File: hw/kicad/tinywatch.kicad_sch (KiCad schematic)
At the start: 18 parts, among them J1 Conn_01x04, J2 Conn_01x30, SW1 SW_Push, SW2 SW_Push, SW3 SW_Push, U1 ATtiny1614-SS

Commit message: R2 hardware
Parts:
- removed R1: 4k7, Resistor_SMD:R_0603_1608Metric_Pad0.98x0.95mm_HandSolder, symbol Device:R
- added C10, C9: 8.2p, Capacitor_SMD:C_0603_1608Metric_Pad1.08x0.95mm_HandSolder, symbol Device:C
- added J3, J4: Conn_01x01_Pin, Connector_Wire:SolderWire-0.25sqmm_1x01_D0.65mm_OD1.7mm, symbol Connector:Conn_01x01_Pin
- added Y1: 32.768 kHz, Crystal:Crystal_DS10_D1.0mm_L4.3mm_Horizontal, symbol Device:Crystal
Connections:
- net GND: now also C10.1, C9.2, J4.1 (Pin_1)
- net VCC: now also J3.1 (Pin_1)
- net VCCQ: now also U1.2 (PA4); no longer U1.11 (PA1)
- net at J1.1 (Pin_1): now also U1.12 (PA2); no longer U1.6 (PB3)
- net at J1.2 (Pin_2): now also U1.11 (PA1); no longer U1.7 (PB2)
- net at J1.3 (Pin_3): now also U1.10 (~{RESET}/PA0)
- new net: C9.1, U1.6 (PB3), Y1.1
- new net: C10.2, U1.7 (PB2), Y1.2
- no-connect marks 1 -> 2
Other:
- moved on the sheet: J1

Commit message: Updated BOM and README
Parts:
- D1: footprint Diode_SMD:D_SOD-110 -> Diode_SMD:D_SOD-123
- J3, J4: now left out of the parts list
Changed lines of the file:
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@@
 	(paper "A4")
 	(junction
+		(at 191.77 71.12)
+		(diameter 0)
+		(color 0 0 0 0)
+	)
+	(junction
 		(at 60.96 78.74)
 		(diameter 0)
@@
 	)
 	(junction
-		(at 191.77 63.5)
-		(diameter 0)
-		(color 0 0 0 0)
-	)
-	(junction
-		(at 191.77 71.12)
+		(at 191.77 101.6)
 		(diameter 0)
 		(color 0 0 0 0)
 	)
 	(junction
-		(at 191.77 101.6)
+		(at 191.77 63.5)
 		(diameter 0)
 		(color 0 0 0 0)
@@
 	(wire
 		(pts
-			(xy 181.61 71.12) (xy 191.77 71.12)
-		)
-		(stroke
-			(width 0)
-			(type default)
-		)
-	)
-	(wire
-		(pts
 			(xy 199.39 106.68) (xy 220.98 106.68)
 		)
@@
 	(wire
 		(pts
+			(xy 191.77 71.12) (xy 205.74 71.12)
+		)
+		(stroke
+			(width 0)
+			(type default)
+		)
+	)
+	(wire
+		(pts
 			(xy 86.36 71.12) (xy 80.01 71.12)
 		)
@@
 	(wire
 		(pts
-			(xy 191.77 71.12) (xy 205.74 71.12)
+			(xy 181.61 71.12) (xy 191.77 71.12)
 		)
 		(stroke
@@
 		(unit 1)
 		(exclude_from_sim no)
-		(in_bom yes)
+		(in_bom no)
 		(on_board yes)
 		(dnp no)
@@
 	)
 	(symbol
+		(lib_name "1N4148W_1")
+		(lib_id "Diode:1N4148W")
+		(at 191.77 67.31 270)
+		(unit 1)
+		(exclude_from_sim no)
+		(in_bom yes)
+		(on_board yes)
+		(dnp no)
+		(fields_autoplaced yes)
+		(property "Reference" "D1"
+			(at 194.31 66.0399 90)
+			(effects
+				(font
+					(size 1.27 1.27)
+				)
+				(justify left)
+			)
+		)
+		(property "Value" "1N4148W"
+			(at 194.31 68.5799 90)
+			(effects
+				(font
+					(size 1.27 1.27)
+				)
+				(justify left)
+			)
+		)
+		(property "Footprint" "Diode_SMD:D_SOD-123"
+			(at 187.325 67.31 0)
+			(effects
+				(font
+					(size 1.27 1.27)
+				)
+				(hide yes)
+			)
+		)
+		(property "Datasheet" "https://www.vishay.com/docs/85748/1n4148w.pdf"
+			(at 191.77 67.31 0)
+			(effects
+				(font
+					(size 1.27 1.27)
+				)
+				(hide yes)
+			)
+		)
+		(property "Description" "75V 0.15A Fast Switching Diode, SOD-123"
+			(at 191.77 67.31 0)
+			(effects
+				(font
+					(size 1.27 1.27)
+				)
+				(hide yes)
+			)
+		)
+		(property "Sim.Device" "D"
+			(at 191.77 67.31 0)
+			(effects
+				(font
+					(size 1.27 1.27)
+				)
+				(hide yes)
+			)
+		)
+		(property "Sim.Pins" "1=K 2=A"
+			(at 191.77 67.31 0)
+			(effects
+				(font
+					(size 1.27 1.27)
+				)
+				(hide yes)
+			)
+		)
+		(pin "2"
+		)
+		(pin "1"
+		)
+		(instances
+			(project "tinywatch"
+				(path "/645abe9d-7b27-45bb-9d9d-6ce483163c39"
+					(reference "D1")
+					(unit 1)
+				)
+			)
+		)
+	)
+	(symbol
 		(lib_id "power:GND")
 		(at 220.98 99.06 270)
@@
 	)
 	(symbol
-		(lib_id "Diode:1N4148W")
-		(at 191.77 67.31 270)
-		(unit 1)
-		(exclude_from_sim no)
-		(in_bom yes)
-		(on_board yes)
-		(dnp no)
-		(fields_autoplaced yes)
-		(property "Reference" "D1"
-			(at 194.31 66.0399 90)
-			(effects
-				(font
-					(size 1.27 1.27)
-				)
-				(justify left)
-			)
-		)
-		(property "Value" "1N4148W"
-			(at 194.31 68.5799 90)
-			(effects
-				(font
-					(size 1.27 1.27)
-				)
-				(justify left)
-			)
-		)
-		(property "Footprint" "Diode_SMD:D_SOD-110"
-			(at 187.325 67.31 0)
-			(effects
-				(font
-					(size 1.27 1.27)
-				)
-				(hide yes)
-			)
-		)
-		(property "Datasheet" "https://www.vishay.com/docs/85748/1n4148w.pdf"
-			(at 191.77 67.31 0)
-			(effects
-				(font
-					(size 1.27 1.27)
-				)
-				(hide yes)
-			)
-		)
-		(property "Description" ""
-			(at 191.77 67.31 0)
-			(effects
-				(font
-					(size 1.27 1.27)
-				)
-				(hide yes)
-			)
-		)
-		(pin "1"
-		)
-		(pin "2"
-		)
-		(instances
-			(project ""
-				(path "/645abe9d-7b27-45bb-9d9d-6ce483163c39"
-					(reference "D1")
-					(unit 1)
-				)
-			)
-		)
-	)
-	(symbol
 		(lib_name "GND_1")
 		(lib_id "power:GND")
@@
 		(unit 1)
 		(exclude_from_sim no)
-		(in_bom yes)
+		(in_bom no)
 		(on_board yes)
 		(dnp no)

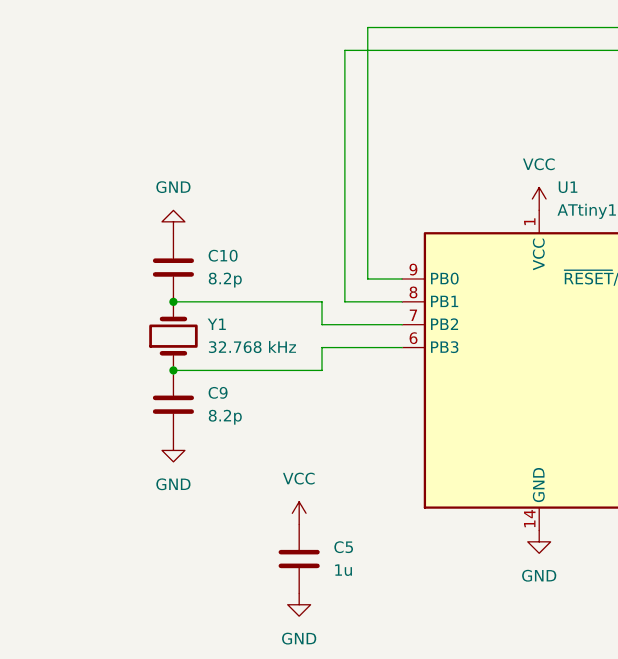
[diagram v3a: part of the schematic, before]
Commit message: Replaced the crystal with a more precise TXCO
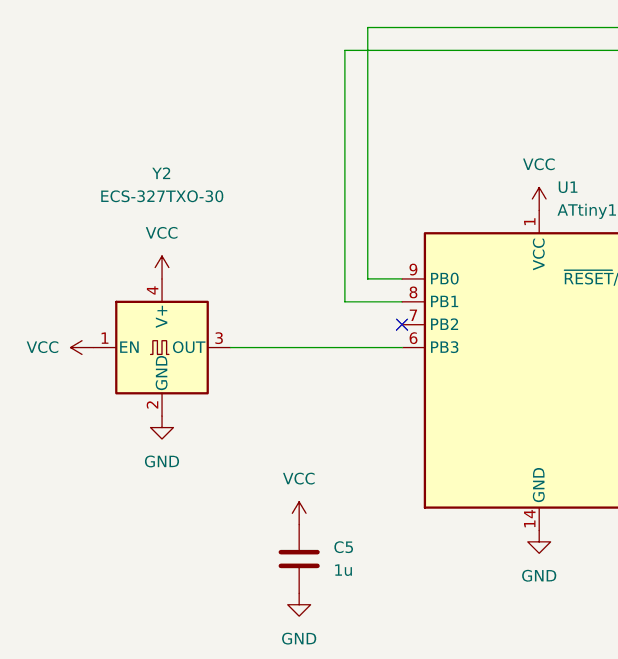
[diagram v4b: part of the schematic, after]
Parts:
- removed C10, C9: 8.2p, Capacitor_SMD:C_0603_1608Metric_Pad1.08x0.95mm_HandSolder, symbol Device:C
- removed Y1: 32.768 kHz, Crystal:Crystal_DS10_D1.0mm_L4.3mm_Horizontal, symbol Device:Crystal
- added Y2: ECS-327TXO-30, Oscillator:Oscillator_SMD_EuroQuartz_XO32-4Pin_3.2x2.5mm, symbol Oscillator:XO32
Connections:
- net GND: now also Y2.2 (GND)
- net VCC: now also Y2.1 (EN), Y2.4 (V+)
- net at U1.6 (PB3): now also Y2.3 (OUT)
- no-connect marks 2 -> 3

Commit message: Replaced TXCO footprint with a more solderable variant
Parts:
- Y2: footprint Oscillator:Oscillator_SMD_EuroQuartz_XO32-4Pin_3.2x2.5mm -> Oscillator:Oscillator_SMD_Abracon_ASE-4Pin_3.2x2.5mm
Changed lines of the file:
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@@
 			)
 		)
-		(property "Footprint" "Oscillator:Oscillator_SMD_EuroQuartz_XO32-4Pin_3.2x2.5mm"
+		(property "Footprint" "Oscillator:Oscillator_SMD_Abracon_ASE-4Pin_3.2x2.5mm"
 			(at 77.47 85.09 0)
 			(effects

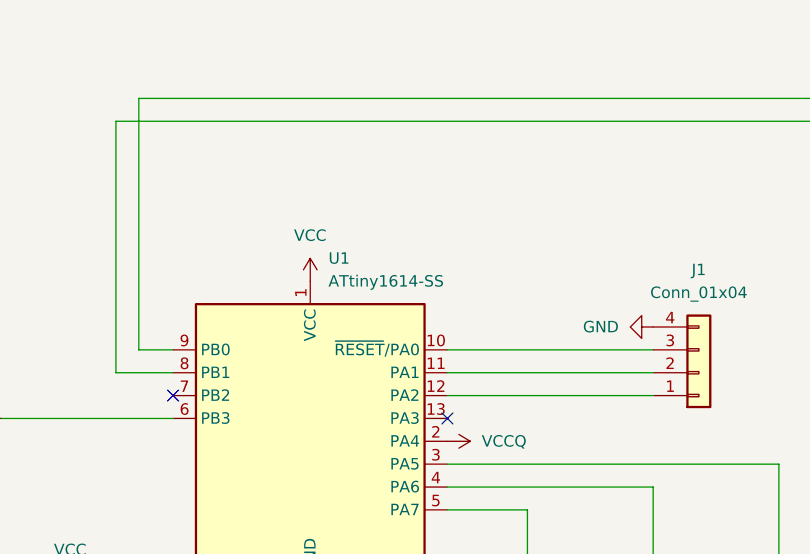
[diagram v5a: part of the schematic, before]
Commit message: Updated to ATtiny3224
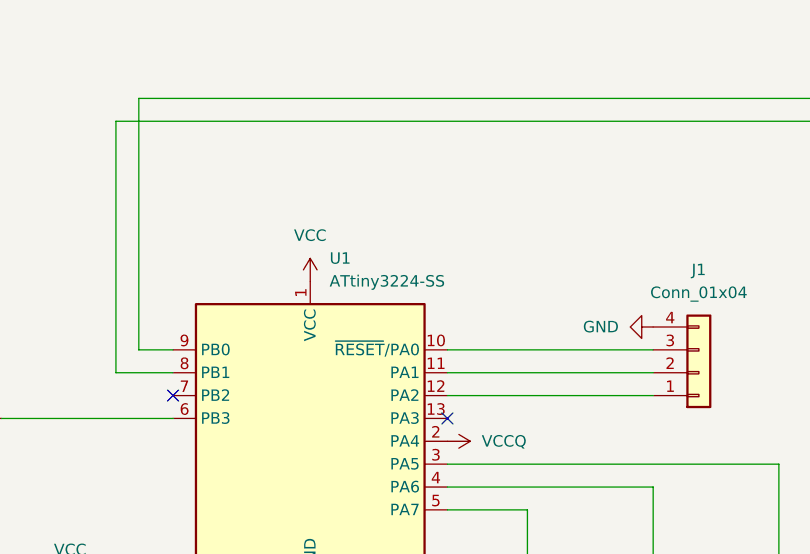
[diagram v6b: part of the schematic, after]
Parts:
- removed U1: ATtiny1614-SS, Package_SO:SOIC-14_3.9x8.7mm_P1.27mm, symbol MCU_Microchip_ATtiny:ATtiny1614-SS
- added U1: ATtiny3224-SS, Package_SO:SOIC-14_3.9x8.7mm_P1.27mm, symbol MCU_Microchip_ATtiny:ATtiny3224-SS
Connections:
- net GND: now also U1.14 (GND)
- net VCC: now also U1.1 (VCC)
- net VCCQ: now also U1.2 (PA4)
- net at J1.1 (Pin_1): now also U1.12 (PA2)
- net at J1.2 (Pin_2): now also U1.11 (PA1)
- net at J1.3 (Pin_3): now also U1.10 (~{RESET}/PA0)
- net at J2.18 (Pin_18): now also U1.9 (PB0)
- net at J2.19 (Pin_19), J2.20 (Pin_20): now also U1.8 (PB1)
- net at SW1.2: now also U1.3 (PA5)
- net at SW2.2: now also U1.4 (PA6)
- net at SW3.2: now also U1.5 (PA7)
- net at Y2.3 (OUT): now also U1.6 (PB3)
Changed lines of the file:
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@@
-	)
-	(symbol
-		(lib_id "MCU_Microchip_ATtiny:ATtiny1614-SS")
-		(at 101.6 78.74 0)
-		(unit 1)
-		(exclude_from_sim no)
-		(in_bom yes)
-		(on_board yes)
-		(dnp no)
-		(fields_autoplaced yes)
-		(property "Reference" "U1"
-			(at 103.6194 58.42 0)
-			(effects
-				(font
-					(size 1.27 1.27)
-				)
-				(justify left)
-			)
-		)
-		(property "Value" "ATtiny1614-SS"
-			(at 103.6194 60.96 0)
-			(effects
-				(font
-					(size 1.27 1.27)
-				)
-				(justify left)
-			)
-		)
-		(property "Footprint" "Package_SO:SOIC-14_3.9x8.7mm_P1.27mm"
-			(at 101.6 78.74 0)
-			(effects
-				(font
-					(size 1.27 1.27)
-					(italic yes)
-				)
-				(hide yes)
-			)
-		)
-		(property "Datasheet" "http://ww1.microchip.com/downloads/en/DeviceDoc/ATtiny1614-data-sheet-40001995A.pdf"
-			(at 101.6 78.74 0)
-			(effects
-				(font
-					(size 1.27 1.27)
-				)
-				(hide yes)
-			)
-		)
-		(property "Description" ""
-			(at 101.6 78.74 0)
-			(effects
-				(font
-					(size 1.27 1.27)
-				)
-				(hide yes)
-			)
-		)
-		(pin "1"
-		)
-		(pin "10"
-		)
-		(pin "11"
-		)
-		(pin "12"
-		)
-		(pin "13"
-		)
-		(pin "14"
-		)
-		(pin "2"
-		)
-		(pin "3"
-		)
-		(pin "4"
-		)
-		(pin "5"
-		)
-		(pin "6"
-		)
-		(pin "7"
-		)
-		(pin "8"
-		)
-		(pin "9"
-		)
-		(instances
-			(project ""
-				(path "/645abe9d-7b27-45bb-9d9d-6ce483163c39"
-					(reference "U1")
-					(unit 1)
-				)
-			)
-		)
 	)
 	(symbol
@@
 					(unit 1)
 				)
+			)
+		)
+	)
+	(symbol
+		(lib_id "MCU_Microchip_ATtiny:ATtiny3224-SS")
+		(at 101.6 78.74 0)
+		(unit 1)
+		(exclude_from_sim no)
+		(in_bom yes)
+		(on_board yes)
+		(dnp no)
+		(fields_autoplaced yes)
+		(property "Reference" "U1"
+			(at 103.7433 58.42 0)
+			(effects
+				(font
+					(size 1.27 1.27)
+				)
+				(justify left)
+			)
+		)
+		(property "Value" "ATtiny3224-SS"
+			(at 103.7433 60.96 0)
+			(effects
+				(font
+					(size 1.27 1.27)
+				)
+				(justify left)
+			)
+		)
+		(property "Footprint" "Package_SO:SOIC-14_3.9x8.7mm_P1.27mm"
+			(at 101.6 78.74 0)
+			(effects
+				(font
+					(size 1.27 1.27)
+					(italic yes)
+				)
+				(hide yes)
+			)
+		)
+		(property "Datasheet" "https://ww1.microchip.com/downloads/en/DeviceDoc/ATtiny3224-3226-3227-Data-Sheet-DS40002345A.pdf"
+			(at 101.6 78.74 0)
+			(effects
+				(font
+					(size 1.27 1.27)
+				)
+				(hide yes)
+			)
+		)
+		(property "Description" "20MHz, 32kB Flash, 3kB SRAM, 256B EEPROM, SOIC-14"
+			(at 101.6 78.74 0)
+			(effects
+				(font
+					(size 1.27 1.27)
+				)
+				(hide yes)
+			)
+		)
+		(pin "13"
+		)
+		(pin "11"
+		)
+		(pin "12"
+		)
+		(pin "4"
+		)
+		(pin "3"
+		)
+		(pin "7"
+		)
+		(pin "2"
+		)
+		(pin "10"
+		)
+		(pin "1"
+		)
+		(pin "6"
+		)
+		(pin "8"
+		)
+		(pin "9"
+		)
+		(pin "5"
+		)
+		(pin "14"
+		)
+		(instances
+			(project ""
+				(path "/645abe9d-7b27-45bb-9d9d-6ce483163c39"
+					(reference "U1")
+					(unit 1)
+				)
